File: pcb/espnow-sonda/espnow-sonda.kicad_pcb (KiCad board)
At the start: 2 copper layers, 62.1 x 25.8 mm, 62 parts, among them J1 , J2 , U1 LTC6269, U2 XC6206P251, U3 LMH6611, U4 XC6902N251

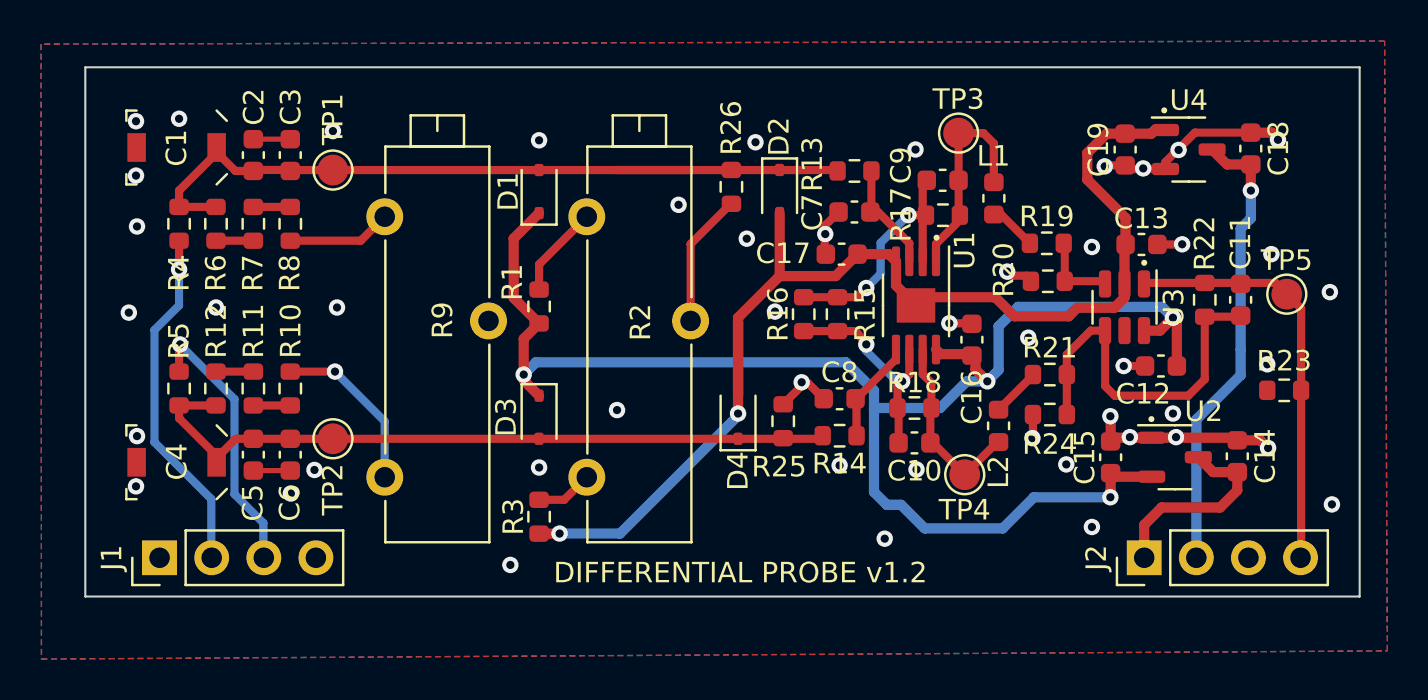
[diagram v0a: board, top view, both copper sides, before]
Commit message: added simulation, updated pcb designs
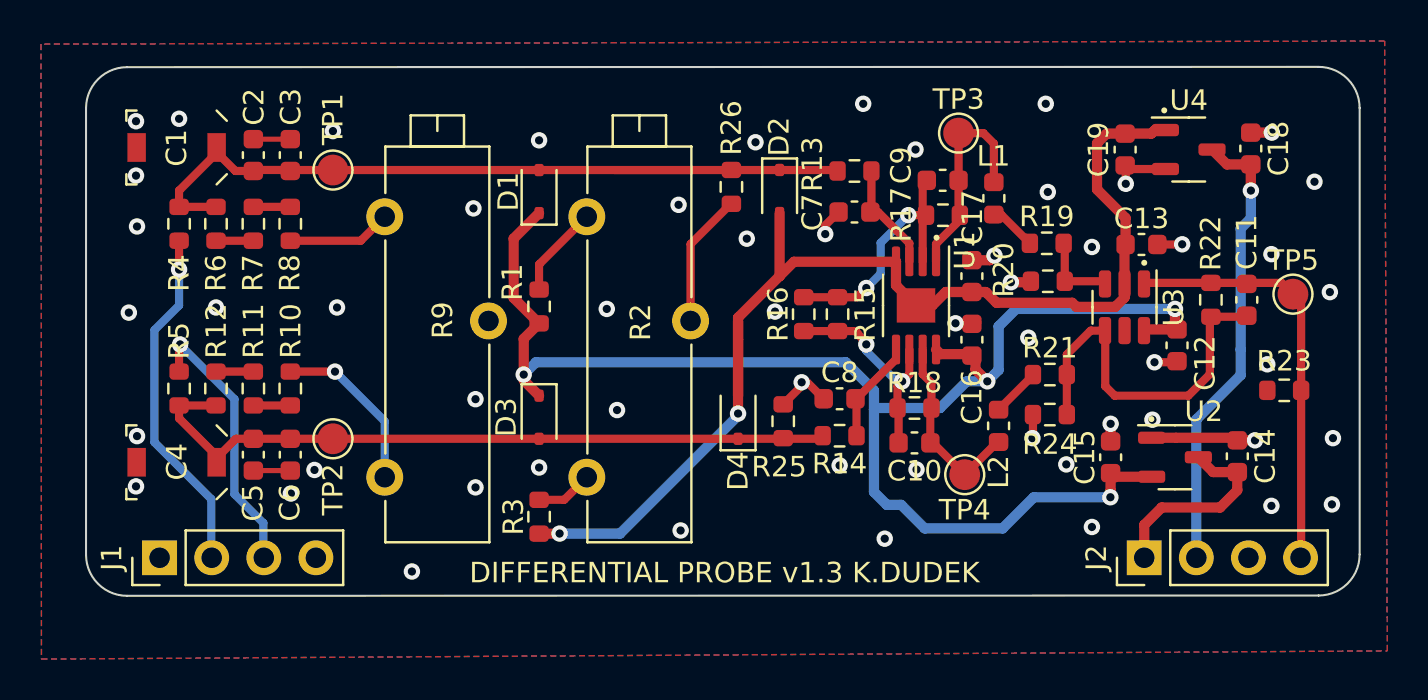
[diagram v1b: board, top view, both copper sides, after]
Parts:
- moved C17 6.44 mm to (89.8, 50.2), turned to -90 degrees
- moved C12 1.28 mm to (99.8, 53.6), turned to 90 degrees
- moved C11 0.30 mm to (103.2, 51.4)
- moved R22 0.30 mm to (101.5, 51.4)
- moved TP5 0.30 mm to (105.5, 51.1)
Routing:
- net GND: track 34.3 -> 24.7 mm, vias 48 -> 56
- net 4V8: track 75.9 -> 74.0 mm
- net -4V8: track 58.8 -> 57.9 mm
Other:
- outline, holes or cut-outs redrawn
- board text added: "DIFFERENTIAL PROBE v1.3 K.DUDEK"
- board text removed: "DIFFERENTIAL PROBE v1.2"
